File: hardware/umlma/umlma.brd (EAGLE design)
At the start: 17.7 x 16.8 mm, 13 parts, among them IC1 TINY25, J1 AVRISP6_TP

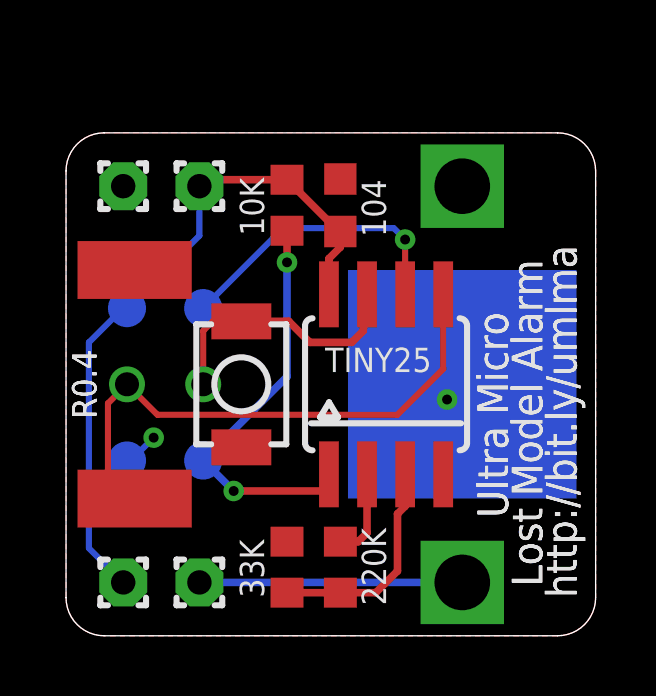
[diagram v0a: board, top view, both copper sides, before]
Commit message: revise mcu pin assignments
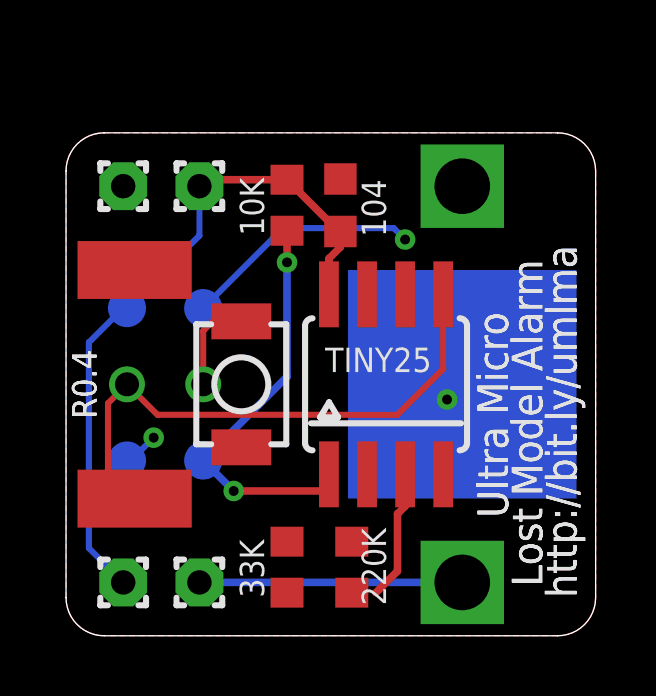
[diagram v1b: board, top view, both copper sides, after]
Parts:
- moved R2 0.38 mm to (9.53, 2.29), turned to 90 degrees
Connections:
- removed net MISO: IC1.6, J1.1
- removed net MOSI: IC1.5, J1.4, SG1.P$5
- removed net N$5: IC1.2, R2.1
- removed net SCK: IC1.7, J1.3, S1.P$2
- removed net VTEST: IC1.3, R2.2, R3.1
- new net ADC: IC1.2, R2.2, R3.1
- new net BUZZA: IC1.7, J1.3, SG1.P$5
- new net BUZZB: IC1.6, J1.1, SG1.P$6
- new net PB0: IC1.5, J1.4, R2.1
- new net SWITCH: IC1.3, S1.P$2
- net GND: no longer SG1.P$6
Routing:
- net MOSI: track 18.5 -> 0.00 mm
- net PB0: track 0.00 -> 17.3 mm
- net MISO: track 9.82 -> 0.00 mm, vias 1 -> 0
- net SCK: track 8.92 -> 0.00 mm
- net BUZZB: track 0.00 -> 7.99 mm, vias 0 -> 1
- net VTEST: track 7.31 -> 0.00 mm
- net SWITCH: track 0.00 -> 4.35 mm
- net N$5: track 2.96 -> 0.00 mm
- net BUZZA: track 0.00 -> 2.23 mm
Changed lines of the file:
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@@
 <layer number="19" name="Unrouted" color="6" fill="1" visible="yes" active="yes"/>
 <layer number="20" name="Dimension" color="15" fill="1" visible="yes" active="yes"/>
-<layer number="21" name="tPlace" color="7" fill="1" visible="no" active="yes"/>
-<layer number="22" name="bPlace" color="7" fill="1" visible="no" active="yes"/>
-<layer number="23" name="tOrigins" color="15" fill="1" visible="no" active="yes"/>
-<layer number="24" name="bOrigins" color="15" fill="1" visible="no" active="yes"/>
-<layer number="25" name="tNames" color="7" fill="1" visible="no" active="yes"/>
-<layer number="26" name="bNames" color="7" fill="1" visible="no" active="yes"/>
-<layer number="27" name="tValues" color="7" fill="1" visible="no" active="yes"/>
-<layer number="28" name="bValues" color="7" fill="1" visible="no" active="yes"/>
-<layer number="29" name="tStop" color="7" fill="3" visible="yes" active="yes"/>
-<layer number="30" name="bStop" color="7" fill="6" visible="yes" active="yes"/>
+<layer number="21" name="tPlace" color="7" fill="1" visible="yes" active="yes"/>
+<layer number="22" name="bPlace" color="7" fill="1" visible="yes" active="yes"/>
+<layer number="23" name="tOrigins" color="15" fill="1" visible="yes" active="yes"/>
+<layer number="24" name="bOrigins" color="15" fill="1" visible="yes" active="yes"/>
+<layer number="25" name="tNames" color="7" fill="1" visible="yes" active="yes"/>
+<layer number="26" name="bNames" color="7" fill="1" visible="yes" active="yes"/>
+<layer number="27" name="tValues" color="7" fill="1" visible="yes" active="yes"/>
+<layer number="28" name="bValues" color="7" fill="1" visible="yes" active="yes"/>
+<layer number="29" name="tStop" color="7" fill="3" visible="no" active="yes"/>
+<layer number="30" name="bStop" color="7" fill="6" visible="no" active="yes"/>
 <layer number="31" name="tCream" color="7" fill="4" visible="no" active="yes"/>
 <layer number="32" name="bCream" color="7" fill="5" visible="no" active="yes"/>
@@
 <layer number="113" name="IDFDebug" color="4" fill="1" visible="no" active="yes"/>
 <layer number="116" name="Patch_BOT" color="9" fill="4" visible="no" active="yes"/>
-<layer number="121" name="tsilk" color="14" fill="1" visible="yes" active="yes"/>
-<layer number="122" name="bsilk" color="6" fill="1" visible="yes" active="yes"/>
+<layer number="121" name="tsilk" color="14" fill="1" visible="no" active="yes"/>
+<layer number="122" name="bsilk" color="6" fill="1" visible="no" active="yes"/>
 <layer number="123" name="tTestmark" color="7" fill="1" visible="no" active="yes"/>
 <layer number="124" name="bTestmark" color="7" fill="1" visible="no" active="yes"/>
@@
 <attribute name="BOM" value="EXCLUDE" x="4.445" y="1.778" size="1.778" layer="27" rot="R270" display="off"/>
 </element>
-<element name="R2" library="rcl" package="R0603" value="220K" x="9.144" y="2.286" smashed="yes" rot="R270">
-<attribute name="PARTNO" value="ERJ-3GEYJ102V" x="9.144" y="2.286" size="1.778" layer="27" rot="R270" display="off"/>
-<attribute name="VALUE" x="10.668" y="1.016" size="0.8128" layer="27" rot="R90"/>
-</element>
 <element name="R3" library="rcl" package="R0603" value="33K" x="7.366" y="2.286" smashed="yes" rot="R90">
 <attribute name="PARTNO" value="ERJ-3GEYJ102V" x="7.366" y="2.286" size="1.778" layer="27" rot="R90" display="off"/>
@@
 <attribute name="BOM" value="EXCLUDE" x="4.445" y="14.986" size="0.8128" layer="27" font="vector" ratio="20" display="off"/>
 <attribute name="VALUE" x="3.429" y="13.681" size="0.8128" layer="28" font="vector" rot="MR180"/>
+</element>
+<element name="R2" library="rcl" package="R0603" value="220K" x="9.525" y="2.286" smashed="yes" rot="R90">
+<attribute name="PARTNO" value="ERJ-3GEYJ102V" x="9.525" y="2.286" size="1.778" layer="27" rot="R90" display="off"/>
+<attribute name="VALUE" x="11.176" y="1.016" size="0.8128" layer="27" rot="R90"/>
 </element>
 </elements>
@@
 <signal name="GND">
 <contactref element="C1" pad="2"/>
-<contactref element="SG1" pad="P$6"/>
-<contactref element="R3" pad="2"/>
 <contactref element="BAT" pad="GND"/>
 <contactref element="J1" pad="6"/>
@@
 <via x="12.7" y="7.874" extent="1-16" drill="0.3302"/>
 <wire x1="13.208" y1="8.382" x2="12.7" y2="7.874" width="0.2032" layer="16"/>
-</signal>
-<signal name="MOSI">
-<contactref element="SG1" pad="P$5"/>
+<contactref element="R3" pad="2"/>
+</signal>
+<signal name="PB0">
 <contactref element="J1" pad="4"/>
 <contactref element="IC1" pad="5"/>
@@
 <wire x1="11.049" y1="7.366" x2="12.573" y2="8.89" width="0.2032" layer="1"/>
 <wire x1="12.573" y1="8.89" x2="12.573" y2="11.382" width="0.2032" layer="1"/>
-<wire x1="2.286" y1="4.572" x2="1.397" y2="5.461" width="0.2032" layer="1"/>
 <wire x1="1.397" y1="5.461" x2="1.397" y2="7.747" width="0.2032" layer="1"/>
 <wire x1="1.397" y1="7.747" x2="2.032" y2="8.382" width="0.2032" layer="1"/>
-</signal>
-<signal name="MISO">
+<contactref element="R2" pad="1"/>
+<wire x1="11.049" y1="7.366" x2="9.525" y2="1.436" width="0" layer="19" extent="1-1"/>
+</signal>
+<signal name="N$2">
+<contactref element="PAD2" pad="1"/>
+<contactref element="BAT" pad="VCC@1"/>
+<wire x1="13.208" y1="1.778" x2="4.445" y2="1.778" width="0.254" layer="16"/>
+</signal>
+<signal name="SWITCH">
+<contactref element="IC1" pad="3"/>
+<wire x1="10.326" y1="1.436" x2="11.049" y2="2.159" width="0.254" layer="1"/>
+<wire x1="11.049" y1="2.159" x2="11.049" y2="4.064" width="0.254" layer="1"/>
+<wire x1="11.049" y1="4.064" x2="11.303" y2="4.318" width="0.254" layer="1"/>
+<wire x1="11.303" y1="4.318" x2="11.303" y2="5.382" width="0.254" layer="1"/>
+<contactref element="S1" pad="P$2"/>
+<wire x1="11.303" y1="5.382" x2="5.842" y2="10.482" width="0" layer="19" extent="1-1"/>
+</signal>
+<signal name="ADC">
+<contactref element="IC1" pad="2"/>
+<contactref element="R3" pad="1"/>
+<contactref element="R2" pad="2"/>
+<wire x1="9.525" y1="3.136" x2="10.033" y2="5.382" width="0" layer="19" extent="1-1"/>
+<wire x1="7.366" y1="1.436" x2="9.525" y2="3.136" width="0" layer="19" extent="1-1"/>
+</signal>
+<signal name="BUZZA">
+<contactref element="IC1" pad="7"/>
+<contactref element="SG1" pad="P$5"/>
+<contactref element="J1" pad="3"/>
+<wire x1="4.894" y1="10.482" x2="4.572" y2="10.16" width="0.2032" layer="1"/>
+<wire x1="4.572" y1="10.16" x2="4.572" y2="8.382" width="0.2032" layer="1"/>
+<wire x1="4.894" y1="10.482" x2="10.033" y2="11.382" width="0" layer="19" extent="1-1"/>
+<wire x1="2.286" y1="4.572" x2="4.572" y2="8.382" width="0" layer="19" extent="1-1"/>
+</signal>
+<signal name="BUZZB">
+<contactref element="SG1" pad="P$6"/>
+<contactref element="IC1" pad="6"/>
 <contactref element="J1" pad="1"/>
-<contactref element="IC1" pad="6"/>
 <wire x1="4.572" y1="10.922" x2="7.239" y2="13.589" width="0.2032" layer="16"/>
 <wire x1="7.239" y1="13.589" x2="10.922" y2="13.589" width="0.2032" layer="16"/>
 <wire x1="10.922" y1="13.589" x2="11.303" y2="13.208" width="0.2032" layer="16"/>
 <via x="11.303" y="13.208" extent="1-16" drill="0.3302"/>
-<wire x1="11.303" y1="13.208" x2="11.303" y2="11.382" width="0.2032" layer="1"/>
-</signal>
-<signal name="SCK">
-<contactref element="J1" pad="3"/>
-<contactref element="S1" pad="P$2"/>
-<contactref element="IC1" pad="7"/>
-<wire x1="10.033" y1="11.382" x2="9.906" y2="10.16" width="0.254" layer="1"/>
-<wire x1="9.906" y1="10.16" x2="9.525" y2="9.779" width="0.254" layer="1"/>
-<wire x1="9.525" y1="9.779" x2="8.128" y2="9.779" width="0.254" layer="1"/>
-<wire x1="5.842" y1="10.482" x2="7.425" y2="10.482" width="0.254" layer="1"/>
-<wire x1="7.425" y1="10.482" x2="8.128" y2="9.779" width="0.254" layer="1"/>
-<wire x1="5.842" y1="10.482" x2="4.894" y2="10.482" width="0.2032" layer="1"/>
-<wire x1="4.894" y1="10.482" x2="4.572" y2="10.16" width="0.2032" layer="1"/>
-<wire x1="4.572" y1="10.16" x2="4.572" y2="8.382" width="0.2032" layer="1"/>
-</signal>
-<signal name="N$2">
-<contactref element="PAD2" pad="1"/>
-<contactref element="BAT" pad="VCC@1"/>
-<wire x1="13.208" y1="1.778" x2="4.445" y2="1.778" width="0.254" layer="16"/>
-</signal>
-<signal name="VTEST">
-<contactref element="R3" pad="1"/>
-<contactref element="R2" pad="2"/>
-<contactref element="IC1" pad="3"/>
-<wire x1="7.366" y1="1.436" x2="9.144" y2="1.436" width="0.254" layer="1"/>
-<wire x1="9.144" y1="1.436" x2="10.326" y2="1.436" width="0.254" layer="1"/>
-<wire x1="10.326" y1="1.436" x2="11.049" y2="2.159" width="0.254" layer="1"/>
-<wire x1="11.049" y1="2.159" x2="11.049" y2="4.064" width="0.254" layer="1"/>
-<wire x1="11.049" y1="4.064" x2="11.303" y2="4.318" width="0.254" layer="1"/>
-<wire x1="11.303" y1="4.318" x2="11.303" y2="5.382" width="0.254" layer="1"/>
-</signal>
-<signal name="N$5">
-<contactref element="R2" pad="1"/>
-<contactref element="IC1" pad="2"/>
-<wire x1="9.144" y1="3.136" x2="9.74" y2="3.136" width="0.254" layer="1"/>
-<wire x1="9.74" y1="3.136" x2="10.033" y2="3.429" width="0.254" layer="1"/>
-<wire x1="10.033" y1="3.429" x2="10.033" y2="5.382" width="0.254" layer="1"/>
+<wire x1="11.303" y1="13.208" x2="11.303" y2="11.382" width="0" layer="19" extent="1-1"/>
+<wire x1="2.286" y1="12.192" x2="4.572" y2="10.922" width="0" layer="19" extent="1-16"/>
 </signal>
 </signals>

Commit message: updated package to correct labeling error
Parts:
- R2: value 220K -> 100K
- R3: value 33K -> 27K
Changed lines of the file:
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@@
 <attribute name="BOM" value="EXCLUDE" x="4.445" y="1.778" size="1.778" layer="27" rot="R270" display="off"/>
 </element>
-<element name="R3" library="rcl" package="R0603" value="33K" x="7.366" y="2.286" smashed="yes" rot="R90">
+<element name="R3" library="rcl" package="R0603" value="27K" x="7.366" y="2.286" smashed="yes" rot="R90">
 <attribute name="PARTNO" value="ERJ-3GEYJ102V" x="7.366" y="2.286" size="1.778" layer="27" rot="R90" display="off"/>
 <attribute name="VALUE" x="6.604" y="1.27" size="0.8128" layer="27" rot="R90"/>
@@
 <attribute name="VALUE" x="3.429" y="13.681" size="0.8128" layer="28" font="vector" rot="MR180"/>
 </element>
-<element name="R2" library="rcl" package="R0603" value="220K" x="9.525" y="2.286" smashed="yes" rot="R90">
+<element name="R2" library="rcl" package="R0603" value="100K" x="9.525" y="2.286" smashed="yes" rot="R90">
 <attribute name="PARTNO" value="ERJ-3GEYJ102V" x="9.525" y="2.286" size="1.778" layer="27" rot="R90" display="off"/>
 <attribute name="VALUE" x="11.176" y="1.016" size="0.8128" layer="27" rot="R90"/>

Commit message: updates to schematic & layout
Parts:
- moved C1 0.38 mm to (9.53, 14.4)
- turned S1 to 270 degrees
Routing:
- net BUZZA: track 2.23 -> 12.9 mm
- net PB0: track 17.3 -> 22.8 mm, vias 0 -> 1
- net ADC: track 0.00 -> 5.32 mm
- net BUZZB: track 7.99 -> 12.0 mm, vias 1 -> 2
- net SWITCH: track 4.35 -> 7.52 mm
- net !RESET: track 14.0 -> 12.1 mm
- net VCC: track 23.0 -> 23.6 mm

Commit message: updated layout, silk, gerbers, zip
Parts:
- added U$1: BTLOGO-LOGO-SM, bt:BTLOGOS
- moved PAD4 0.28 mm to (4.32, 14.7)
- moved PAD3 0.28 mm to (1.78, 14.7)
- moved PAD2 0.28 mm to (4.32, 2.03)
- moved PAD1 0.28 mm to (1.78, 2.03)
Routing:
- net VCC: track 23.6 -> 23.0 mm
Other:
- board text added: "bit.ly/umlma"
